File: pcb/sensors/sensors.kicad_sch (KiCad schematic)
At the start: 10 parts, among them J1 5V POWER, J10 PRESSURE, U1 XIAO ESP32-S3 / SOCKETED, U6 ADS1115IDGSR

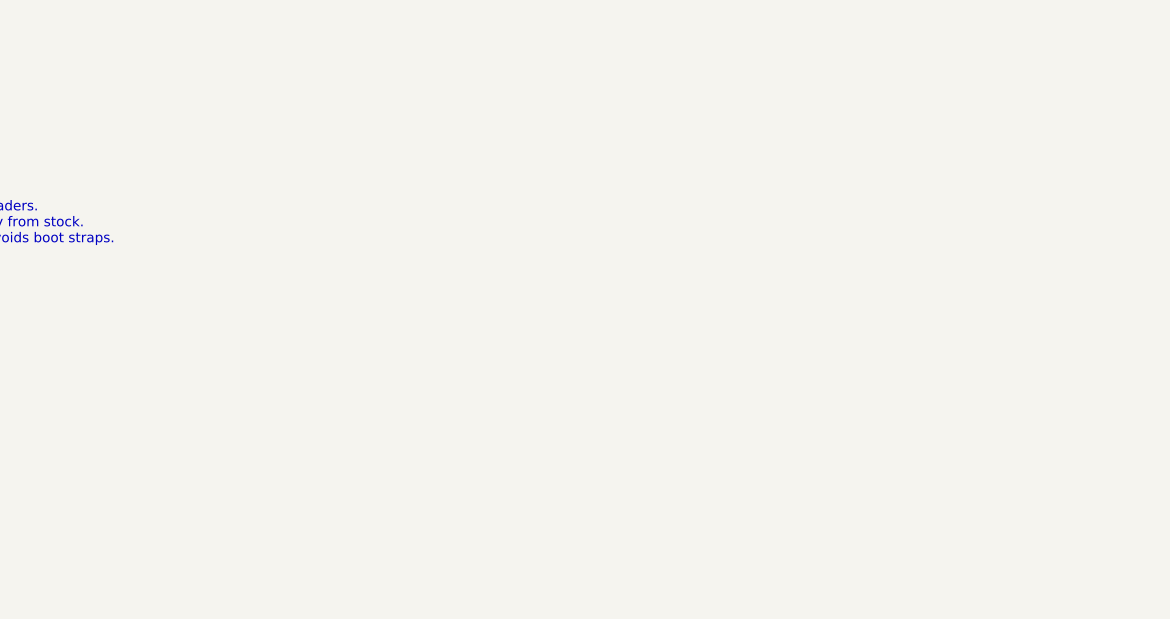
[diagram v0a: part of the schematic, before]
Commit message: Have JLCPCB solder the XIAO sockets and refresh sensors manufacturing
U1, the XIAO, stays in the schematic for its pinout but leaves the board.
Two female 1x7 sockets, J11 (XIAO pins 1-7) and J12 (pins 8-14), take its
fourteen holes with the same nets, so the routing is unchanged. They use
HX PM2.54-1x7P ZC-Y (C22438157) on a local footprint that keeps the tight
courtyard of the old U1 footprint; the XIAO outline becomes board silkscreen.

Bring sourcing and the BOM up to the XIAO board: drop the twenty
ESP32-S3-MINI parts, source C13-C15, J10, R26, U6 and the sockets, move D2
to the 0805 KT-0805G, refresh the catalog snapshot, and skip off-board
symbols in generate_bom.py. Rewrite customize-manufacturing.py for the J1-J12
references, without aliases or parity exceptions. The JLCPCB preview
confirmed every placement, with U6 and the sockets at +270 degrees and D2
without correction. Remove the files of the old export chain.

Co-Authored-By: Claude Opus 5.5 <noreply@anthropic.com>
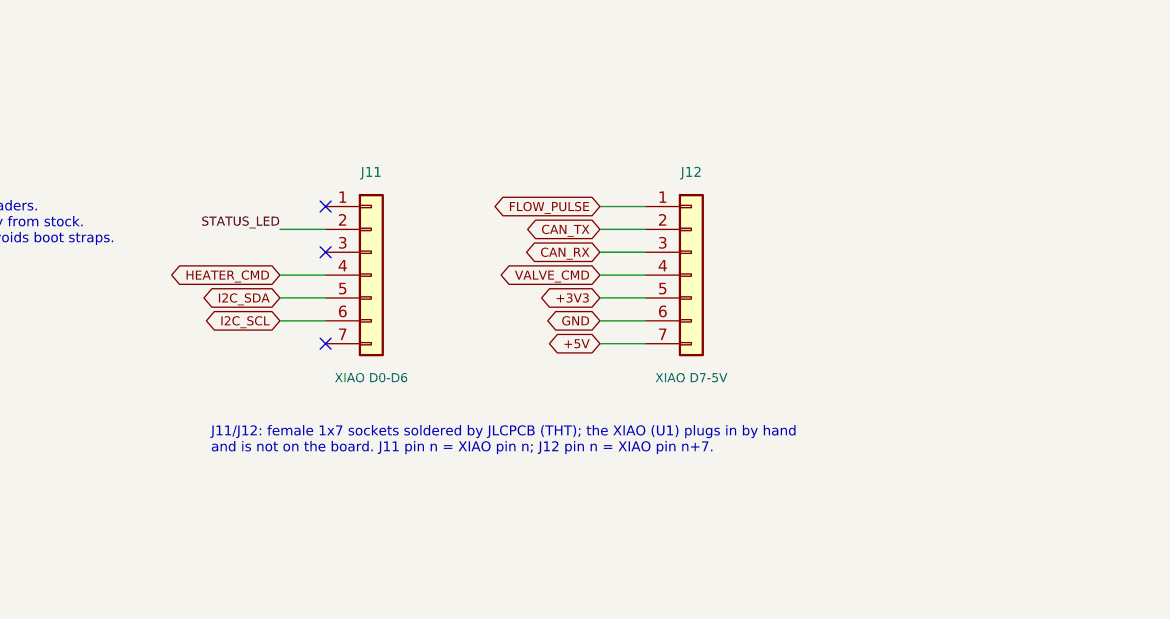
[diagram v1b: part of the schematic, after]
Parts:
- added J11: XIAO D0-D6, Sensors_Local:XIAO_Socket_1x07_P2.54mm_Vertical, symbol Connector_Generic:Conn_01x07
- added J12: XIAO D7-5V, Sensors_Local:XIAO_Socket_1x07_P2.54mm_Vertical, symbol Connector_Generic:Conn_01x07
- U1: now left out of the parts list
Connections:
- net +3V3: now also J12.5 (Pin_5)
- net +5V: now also J12.7 (Pin_7)
- net CAN_RX: now also J12.3 (Pin_3)
- net CAN_TX: now also J12.2 (Pin_2)
- net FLOW_PULSE: now also J12.1 (Pin_1)
- net GND: now also J12.6 (Pin_6)
- net HEATER_CMD: now also J11.4 (Pin_4)
- net I2C_SCL: now also J11.6 (Pin_6)
- net I2C_SDA: now also J11.5 (Pin_5)
- net STATUS_LED: now also J11.2 (Pin_2)
- net VALVE_CMD: now also J12.4 (Pin_4)
- no-connect marks 17 -> 20
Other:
- note added: "J11/J12: female 1x7 sockets soldered by JLCPCB (THT); the XIAO (U1) plugs in by hand and is not on the board. J11 pin n = XIAO pin n; J12 pin n = XIAO pin n+7."

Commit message: Add an M2.5 mounting hole to the sensors board
H1 is a 2.7mm NPTH mounting hole for an M2.5 screw into a brass insert in
the printed enclosure, so the GND pour under the screw head needs no
keepout. The symbol stays out of the BOM, and generate_bom.py now skips
symbols excluded from the BOM so the hole does not break the UUID check.

Co-Authored-By: Claude Opus 5.5 <noreply@anthropic.com>
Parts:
- added H1: M2.5, MountingHole:MountingHole_2.7mm_M2.5, symbol Mechanical:MountingHole
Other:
- note added: "H1: M2.5 mounting hole, 2.7mm NPTH, not connected."
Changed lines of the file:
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@@
 (global_label "+5V" (shape bidirectional) (at 283.21 172.72 180) (effects (font (size 1.0 1.0)) (justify right)) (property "Intersheetrefs" "${INTERSHEET_REFS}" (at 283.21 172.72 180) (effects (font (size 1.0 1.0)) (hide yes))))
 (text "J11/J12: female 1x7 sockets soldered by JLCPCB (THT); the XIAO (U1) plugs in by hand\nand is not on the board. J11 pin n = XIAO pin n; J12 pin n = XIAO pin n+7." (at 240 182 0) (effects (font (size 1.1 1.1)) (justify left top)))
+(symbol (lib_id "Mechanical:MountingHole") (at 322.58 233.68 0) (unit 1) (exclude_from_sim no) (in_bom no) (on_board yes) (dnp no) (property "Reference" "H1" (at 327.58 231.68 0) (effects (font (size 1.1 1.1)) (justify left))) (property "Value" "M2.5" (at 327.58 234.68 0) (effects (font (size 1.0 1.0)) (justify left))) (property "Footprint" "MountingHole:MountingHole_2.7mm_M2.5" (at 322.58 233.68 0) (effects (font (size 1.0 1.0)) (justify left)) (hide yes)) (property "Datasheet" "" (at 322.58 233.68 0) (effects (font (size 1.0 1.0)) (justify left)) (hide yes)) (property "Description" "Mounting Hole without connection" (at 322.58 233.68 0) (effects (font (size 1.0 1.0)) (justify left)) (hide yes)) (property "MPN" "M2.5 / 2.7mm" (at 322.58 233.68 0) (effects (font (size 1.0 1.0)) (justify left)) (hide yes)) (instances (project "sensors" (path "/655ba0f3-0427-5cf4-88d9-0bb38b1023d4" (reference "H1") (unit 1)))))
+(text "H1: M2.5 mounting hole, 2.7mm NPTH, not connected." (at 320 245 0) (effects (font (size 1.1 1.1)) (justify left top)))
 (sheet_instances (path "/" (page "1")))
 (embedded_fonts no)
